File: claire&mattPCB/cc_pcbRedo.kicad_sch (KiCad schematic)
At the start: 89 parts, among them J1 Conn_02x05_Odd_Even, J2 Micro_SD_Card_Det_Hirose_DM3AT, J3 4x4 Keypad, J4 DC-DC_JUMPER, J5 PS_WIRES, J6 PS_BJ, J7 DC-DC Converter, SW1 SW_Push, U1 ESP8266, U2 7in_display_controller, U3 RFID_Scanner, U4 TFT_2.8IN_DISPLAY, U5 74HC14, U6 STM32F091RCTx, U7 MEZD71201AF, U8 TPS56325x, U9 4N28

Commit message: minor changes
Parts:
- added R29: (no value), Resistor_SMD:R_0805_2012Metric_Pad1.20x1.40mm_HandSolder, symbol Device:R_US
- C13: value (none) -> 10uF; footprint (none) -> Capacitor_SMD:C_0805_2012Metric_Pad1.18x1.45mm_HandSolder
- C9: value (none) -> 2.2uf; footprint (none) -> Capacitor_SMD:C_0805_2012Metric_Pad1.18x1.45mm_HandSolder
- H1, H2, H3, H4: footprint (none) -> imported_footprints:MountingHole_8.4mm
- H10, H5, H6, H7, H8, H9: footprint (none) -> imported_footprints:MountingHole_2.2mm
- L1: footprint (none) -> imported_footprints:irl_toroid_inductor
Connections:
- net 9_GND: now also R29.2
- net VAC_GND: now also R29.1
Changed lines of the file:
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@@
   (junction (at 220.98 73.66) (diameter 0) (color 0 0 0 0)
   )
-  (junction (at 262.89 50.8) (diameter 0) (color 0 0 0 0)
-  )
   (junction (at 189.23 17.78) (diameter 0) (color 0 0 0 0)
   )
+  (junction (at 266.7 50.8) (diameter 0) (color 0 0 0 0)
+  )
   (junction (at 254 100.33) (diameter 0) (color 0 0 0 0)
   )
@@
   (junction (at 72.39 158.75) (diameter 0) (color 0 0 0 0)
   )
+  (junction (at 260.35 50.8) (diameter 0) (color 0 0 0 0)
+  )
   (junction (at 279.4 88.9) (diameter 0) (color 0 0 0 0)
   )
@@
   (junction (at 160.02 184.15) (diameter 0) (color 0 0 0 0)
   )
+  (junction (at 229.87 38.1) (diameter 0) (color 0 0 0 0)
+  )
   (junction (at 39.37 57.15) (diameter 0) (color 0 0 0 0)
   )
@@
     (stroke (width 0) (type default) (color 0 0 0 0))
   )
+  (wire (pts (xy 248.92 53.34) (xy 229.87 53.34))
+    (stroke (width 0) (type default) (color 0 0 0 0))
+  )
   (wire (pts (xy 135.89 156.21) (xy 135.89 147.32))
     (stroke (width 0) (type default) (color 0 0 0 0))
@@
     (stroke (width 0) (type default) (color 0 0 0 0))
   )
-  (polyline (pts (xy 180.34 57.15) (xy 284.48 57.15))
+  (polyline (pts (xy 180.34 58.42) (xy 284.48 58.42))
     (stroke (width 0) (type default) (color 0 0 0 0))
   )
@@
     (stroke (width 0) (type default) (color 0 0 0 0))
   )
-  (wire (pts (xy 262.89 50.8) (xy 266.7 50.8))
-    (stroke (width 0) (type default) (color 0 0 0 0))
-  )
   (wire (pts (xy 189.23 52.07) (xy 194.31 52.07))
     (stroke (width 0) (type default) (color 0 0 0 0))
@@
     (stroke (width 0) (type default) (color 0 0 0 0))
   )
-  (wire (pts (xy 260.35 50.8) (xy 262.89 50.8))
-    (stroke (width 0) (type default) (color 0 0 0 0))
-  )
   (wire (pts (xy 276.86 21.59) (xy 276.86 20.32))
     (stroke (width 0) (type default) (color 0 0 0 0))
@@
     (stroke (width 0) (type default) (color 0 0 0 0))
   )
-  (wire (pts (xy 262.89 50.8) (xy 262.89 53.34))
+  (wire (pts (xy 260.35 50.8) (xy 266.7 50.8))
     (stroke (width 0) (type default) (color 0 0 0 0))
   )
@@
     (stroke (width 0) (type default) (color 0 0 0 0))
   )
+  (wire (pts (xy 260.35 50.8) (xy 259.08 50.8))
+    (stroke (width 0) (type default) (color 0 0 0 0))
+  )
   (wire (pts (xy 250.19 100.33) (xy 254 100.33))
     (stroke (width 0) (type default) (color 0 0 0 0))
@@
     (stroke (width 0) (type default) (color 0 0 0 0))
   )
-  (wire (pts (xy 227.33 38.1) (xy 245.11 38.1))
+  (wire (pts (xy 227.33 38.1) (xy 229.87 38.1))
     (stroke (width 0) (type default) (color 0 0 0 0))
   )
@@
     (stroke (width 0) (type default) (color 0 0 0 0))
   )
+  (wire (pts (xy 266.7 50.8) (xy 270.51 50.8))
+    (stroke (width 0) (type default) (color 0 0 0 0))
+  )
   (wire (pts (xy 26.67 171.45) (xy 34.29 171.45))
     (stroke (width 0) (type default) (color 0 0 0 0))
@@
     (stroke (width 0) (type default) (color 0 0 0 0))
   )
+  (wire (pts (xy 259.08 53.34) (xy 256.54 53.34))
+    (stroke (width 0) (type default) (color 0 0 0 0))
+  )
   (wire (pts (xy 146.05 22.86) (xy 148.59 22.86))
     (stroke (width 0) (type default) (color 0 0 0 0))
@@
     (stroke (width 0) (type default) (color 0 0 0 0))
   )
+  (wire (pts (xy 229.87 38.1) (xy 245.11 38.1))
+    (stroke (width 0) (type default) (color 0 0 0 0))
+  )
   (wire (pts (xy 241.3 137.16) (xy 248.92 137.16))
     (stroke (width 0) (type default) (color 0 0 0 0))
@@
     (stroke (width 0) (type default) (color 0 0 0 0))
   )
+  (wire (pts (xy 259.08 50.8) (xy 259.08 53.34))
+    (stroke (width 0) (type default) (color 0 0 0 0))
+  )
+  (wire (pts (xy 229.87 53.34) (xy 229.87 38.1))
+    (stroke (width 0) (type default) (color 0 0 0 0))
+  )
   (wire (pts (xy 151.13 147.32) (xy 152.4 147.32))
     (stroke (width 0) (type default) (color 0 0 0 0))
@@
     )
   )
-  (global_label "9_GND" (shape input) (at 262.89 53.34 0) (fields_autoplaced)
+  (global_label "9_GND" (shape input) (at 270.51 50.8 0) (fields_autoplaced)
     (effects (font (size 1.27 1.27)) (justify left))
-    (property "Intersheet References" "${INTERSHEET_REFS}" (id 0) (at 271.3507 53.4194 0)
+    (property "Intersheet References" "${INTERSHEET_REFS}" (id 0) (at 278.9707 50.8794 0)
       (effects (font (size 1.27 1.27)) (justify left) hide)
     )
@@
       (effects (font (size 1.27 1.27)) (justify left))
     )
-    (property "Footprint" "" (id 2) (at 106.68 22.86 0)
+    (property "Footprint" "imported_footprints:MountingHole_8.4mm" (id 2) (at 106.68 22.86 0)
       (effects (font (size 1.27 1.27)) hide)
     )
@@
     (pin "2")
   )
+  (symbol (lib_id "Device:R_US") (at 252.73 53.34 90) (unit 1)
+    (in_bom yes) (on_board yes)
+    (property "Reference" "R29" (id 0) (at 252.73 50.8 90))
+    (property "Value" "" (id 1) (at 252.73 56.2356 90))
+    (property "Footprint" "Resistor_SMD:R_0805_2012Metric_Pad1.20x1.40mm_HandSolder" (id 2) (at 252.984 52.324 90)
+      (effects (font (size 1.27 1.27)) hide)
+    )
+    (property "Datasheet" "" (id 3) (at 252.73 53.34 0)
+      (effects (font (size 1.27 1.27)) hide)
+    )
+    (pin "1")
+    (pin "2")
+  )
   (symbol (lib_id "Mechanical:MountingHole") (at 182.88 77.47 0) (unit 1)
     (in_bom yes) (on_board yes) (fields_autoplaced)
@@
       (effects (font (size 1.27 1.27)) (justify left))
     )
-    (property "Footprint" "" (id 2) (at 182.88 77.47 0)
+    (property "Footprint" "imported_footprints:MountingHole_2.2mm" (id 2) (at 182.88 77.47 0)
       (effects (font (size 1.27 1.27)) hide)
     )
@@
       (effects (font (size 1.27 1.27)) (justify left))
     )
-    (property "Footprint" "" (id 2) (at 15.24 125.73 0)
+    (property "Footprint" "imported_footprints:MountingHole_2.2mm" (id 2) (at 15.24 125.73 0)
       (effects (font (size 1.27 1.27)) hide)
     )
@@
       (effects (font (size 1.27 1.27)) (justify left))
     )
-    (property "Footprint" "" (id 2) (at 106.68 35.56 0)
+    (property "Footprint" "imported_footprints:MountingHole_8.4mm" (id 2) (at 106.68 35.56 0)
       (effects (font (size 1.27 1.27)) hide)
     )
@@
       (effects (font (size 1.27 1.27)) (justify left))
     )
-    (property "Value" "" (id 1) (at 172.72 138.43 90)
+    (property "Value" "2.2uf" (id 1) (at 172.72 138.43 90)
       (effects (font (size 1.27 1.27)) (justify left))
     )
-    (property "Footprint" "" (id 2) (at 170.4848 139.7 0)
+    (property "Footprint" "Capacitor_SMD:C_0805_2012Metric_Pad1.18x1.45mm_HandSolder" (id 2) (at 170.4848 139.7 0)
       (effects (font (size 1.27 1.27)) hide)
     )
@@
       (effects (font (size 1.27 1.27)) (justify left))
     )
-    (property "Footprint" "" (id 2) (at 196.85 81.28 0)
+    (property "Footprint" "imported_footprints:MountingHole_2.2mm" (id 2) (at 196.85 81.28 0)
       (effects (font (size 1.27 1.27)) hide)
     )
@@
     (property "Reference" "L1" (id 0) (at 252.73 15.24 0))
     (property "Value" "1m" (id 1) (at 252.73 17.78 0))
-    (property "Footprint" "" (id 2) (at 252.73 21.59 0)
+    (property "Footprint" "imported_footprints:irl_toroid_inductor" (id 2) (at 252.73 21.59 0)
       (effects (font (size 1.27 1.27)) hide)
     )
@@
       (effects (font (size 1.27 1.27)) (justify left))
     )
-    (property "Footprint" "" (id 2) (at 106.68 29.21 0)
+    (property "Footprint" "imported_footprints:MountingHole_8.4mm" (id 2) (at 106.68 29.21 0)
       (effects (font (size 1.27 1.27)) hide)
     )
@@
       (effects (font (size 1.27 1.27)) (justify left))
     )
-    (property "Footprint" "" (id 2) (at 106.68 16.51 0)
+    (property "Footprint" "imported_footprints:MountingHole_8.4mm" (id 2) (at 106.68 16.51 0)
       (effects (font (size 1.27 1.27)) hide)
     )
@@
       (effects (font (size 1.27 1.27)) (justify left))
     )
-    (property "Footprint" "" (id 2) (at 15.24 133.35 0)
+    (property "Footprint" "imported_footprints:MountingHole_2.2mm" (id 2) (at 15.24 133.35 0)
       (effects (font (size 1.27 1.27)) hide)
     )
@@
       (effects (font (size 1.27 1.27)) (justify left))
     )
-    (property "Footprint" "" (id 2) (at 34.29 125.73 0)
+    (property "Footprint" "imported_footprints:MountingHole_2.2mm" (id 2) (at 34.29 125.73 0)
       (effects (font (size 1.27 1.27)) hide)
     )
@@
       (effects (font (size 1.27 1.27)) (justify left))
     )
-    (property "Value" "" (id 1) (at 218.44 81.28 0)
+    (property "Value" "10uF" (id 1) (at 218.44 81.28 0)
       (effects (font (size 1.27 1.27)) (justify left))
     )
-    (property "Footprint" "" (id 2) (at 220.0148 83.82 0)
+    (property "Footprint" "Capacitor_SMD:C_0805_2012Metric_Pad1.18x1.45mm_HandSolder" (id 2) (at 220.0148 83.82 0)
       (effects (font (size 1.27 1.27)) hide)
     )
@@
       (effects (font (size 1.27 1.27)) (justify left))
     )
-    (property "Footprint" "" (id 2) (at 34.29 133.35 0)
+    (property "Footprint" "imported_footprints:MountingHole_2.2mm" (id 2) (at 34.29 133.35 0)
       (effects (font (size 1.27 1.27)) hide)
     )
@@
       (reference "R28") (unit 1) (value "300") (footprint "Resistor_SMD:R_0805_2012Metric_Pad1.20x1.40mm_HandSolder")
     )
+    (path "/163b4f02-ce0e-491d-9e96-bb78a94d495b"
+      (reference "R29") (unit 1) (value "0") (footprint "Resistor_SMD:R_0805_2012Metric_Pad1.20x1.40mm_HandSolder")
+    )
     (path "/ffb85886-0f4e-471b-9049-c50690319492"

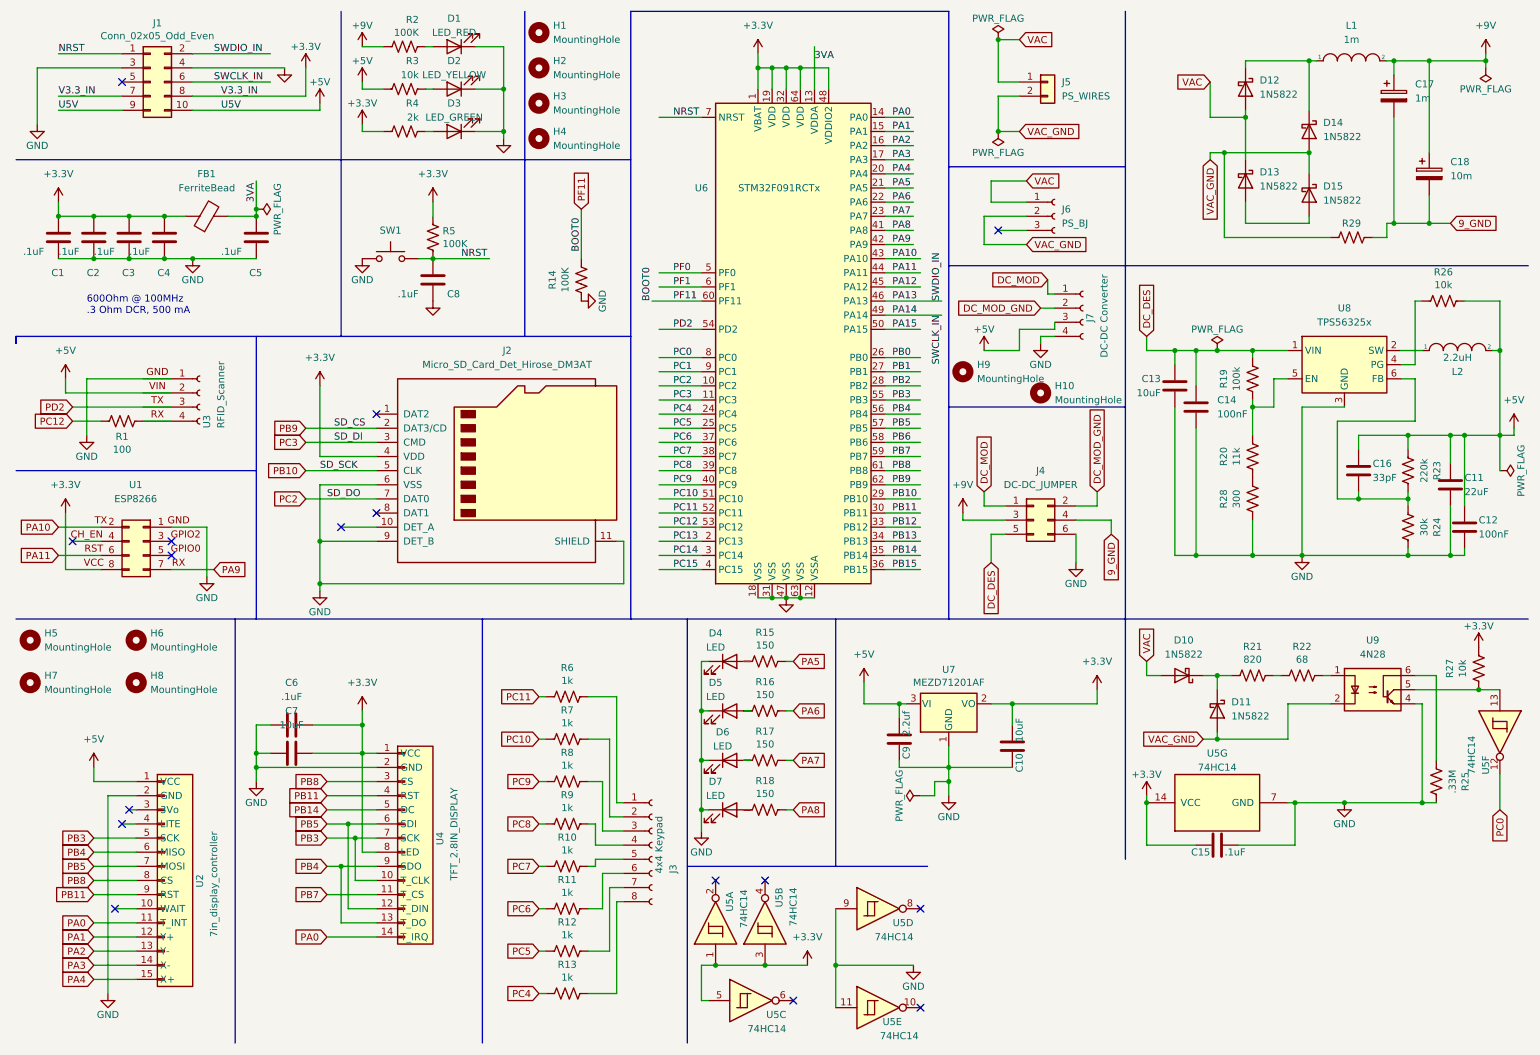
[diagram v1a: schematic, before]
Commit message: updated schematic with text descriptions for each block. Also, added 0 ohm resistor and 10 ohm current limiting resistor to pcb. Minor changes were made to the designed buck converter circuit.
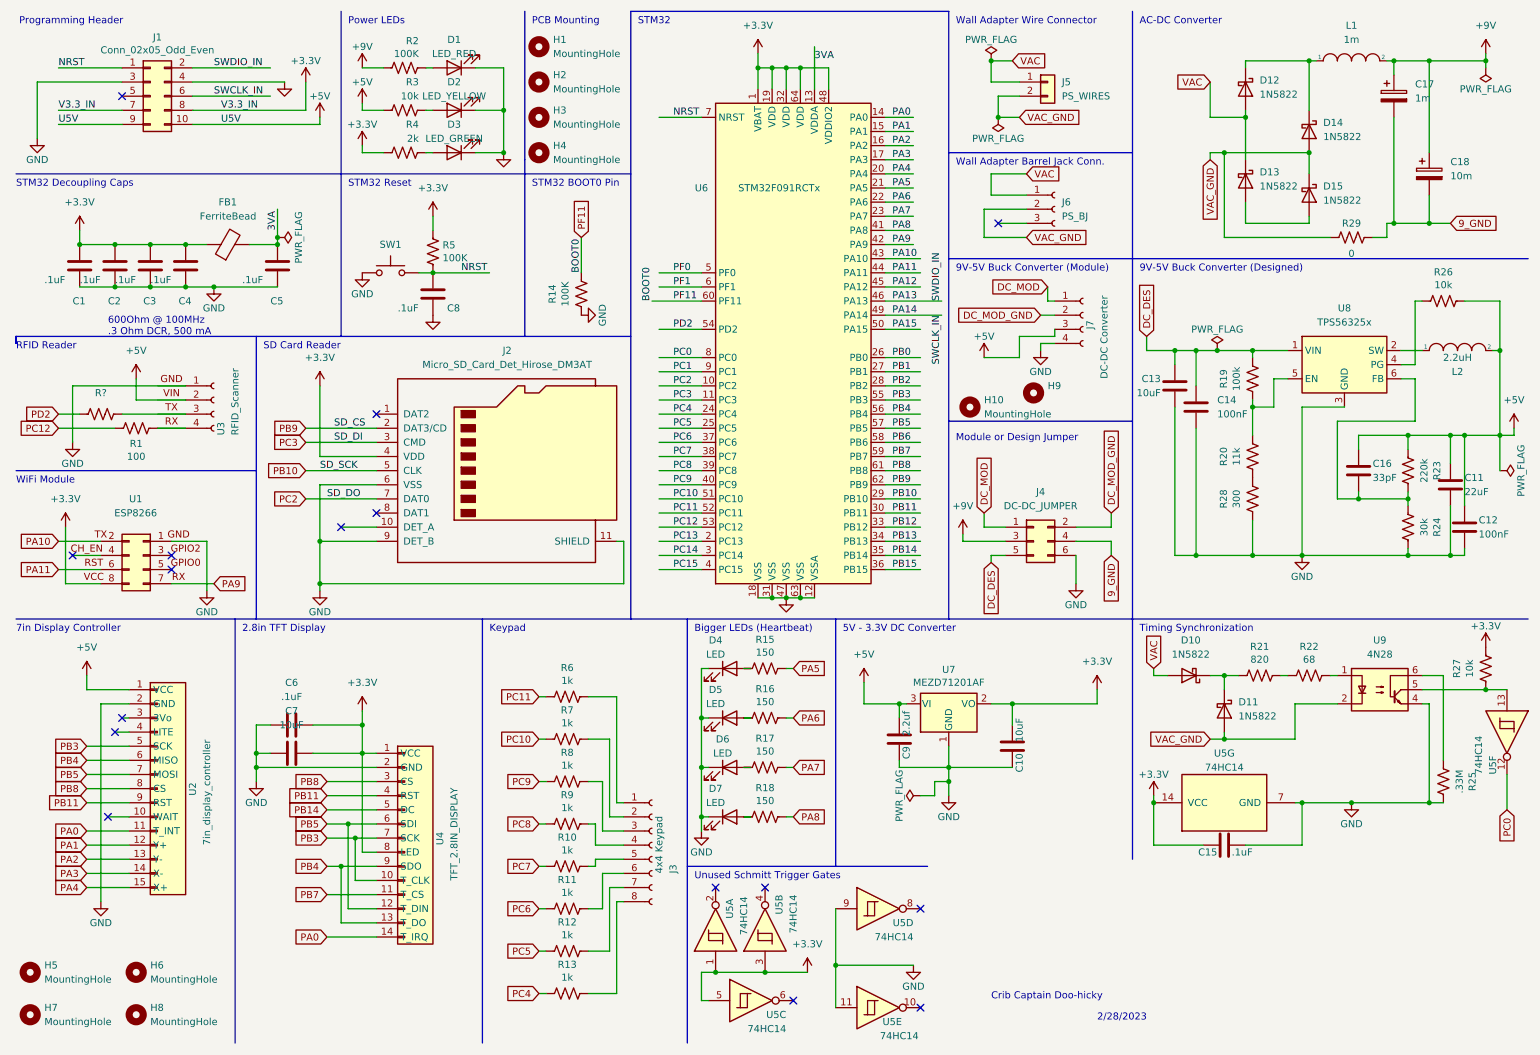
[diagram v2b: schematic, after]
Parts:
- added R?: (no value), Resistor_SMD:R_0805_2012Metric_Pad1.20x1.40mm_HandSolder, symbol Device:R_US
- H9: value MountingHole -> (none); footprint imported_footprints:MountingHole_2.2mm -> (none)
- R29: value (none) -> 0
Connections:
- net PD2: now also R?.1; no longer U3.3
- new net: R?.2, U3.3
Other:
- note added: "2.8in TFT Display"
- note added: "2/28/2023"
- note added: "5V - 3.3V DC Converter"
- note added: "7in Display Controller"
- note added: "9V-5V Buck Converter (Designed)"
- note added: "9V-5V Buck Converter (Module)"
- note added: "AC-DC Converter"
- note added: "Bigger LEDs (Heartbeat)"
- note added: "Crib Captain Doo-hicky"
- note added: "Keypad"
- note added: "Module or Design Jumper"
- note added: "PCB Mounting"
- note added: "Power LEDs"
- note added: "Programming Header"
- note added: "RFID Reader"
- note added: "SD Card Reader"
- note added: "STM32"
- note added: "STM32 BOOT0 Pin"
- note added: "STM32 Decoupling Caps"
- note added: "STM32 Reset"
- note added: "Timing Synchronization"
- note added: "Unused Schmitt Trigger Gates"
- note added: "Wall Adapter Barrel Jack Conn."
- note added: "Wall Adapter Wire Connector"
- note added: "WiFi Module"
- moved on the sheet: C1, C15, C2, C3, C4, C5, C8, D1, D10, D11, D2, D3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

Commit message: no DRC warnings
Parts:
- gave numbers to parts that had none: 1
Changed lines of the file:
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@@
   (symbol (lib_id "Device:R_US") (at 27.94 85.09 90) (unit 1)
     (in_bom yes) (on_board yes)
-    (property "Reference" "R?" (id 0) (at 27.94 81.28 90))
+    (property "Reference" "R30" (id 0) (at 27.94 81.28 90))
     (property "Value" "" (id 1) (at 27.94 82.55 90))
     (property "Footprint" "Resistor_SMD:R_0805_2012Metric_Pad1.20x1.40mm_HandSolder" (id 2) (at 28.194 84.074 90)
@@
     )
     (path "/144ff530-b485-4099-8683-178b3d988ffd"
-      (reference "R?") (unit 1) (value "10") (footprint "Resistor_SMD:R_0805_2012Metric_Pad1.20x1.40mm_HandSolder")
+      (reference "R30") (unit 1) (value "10") (footprint "Resistor_SMD:R_0805_2012Metric_Pad1.20x1.40mm_HandSolder")
     )
     (path "/ffb85886-0f4e-471b-9049-c50690319492"
